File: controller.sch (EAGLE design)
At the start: 47 parts, among them IC1 7805DT, Q3 MOSFET-NCHANNELFDD8780, Q5 MMBT4403, SW1 ROTARTY_ENCODER, U1 ATMEGA328P, Y1 16MHz

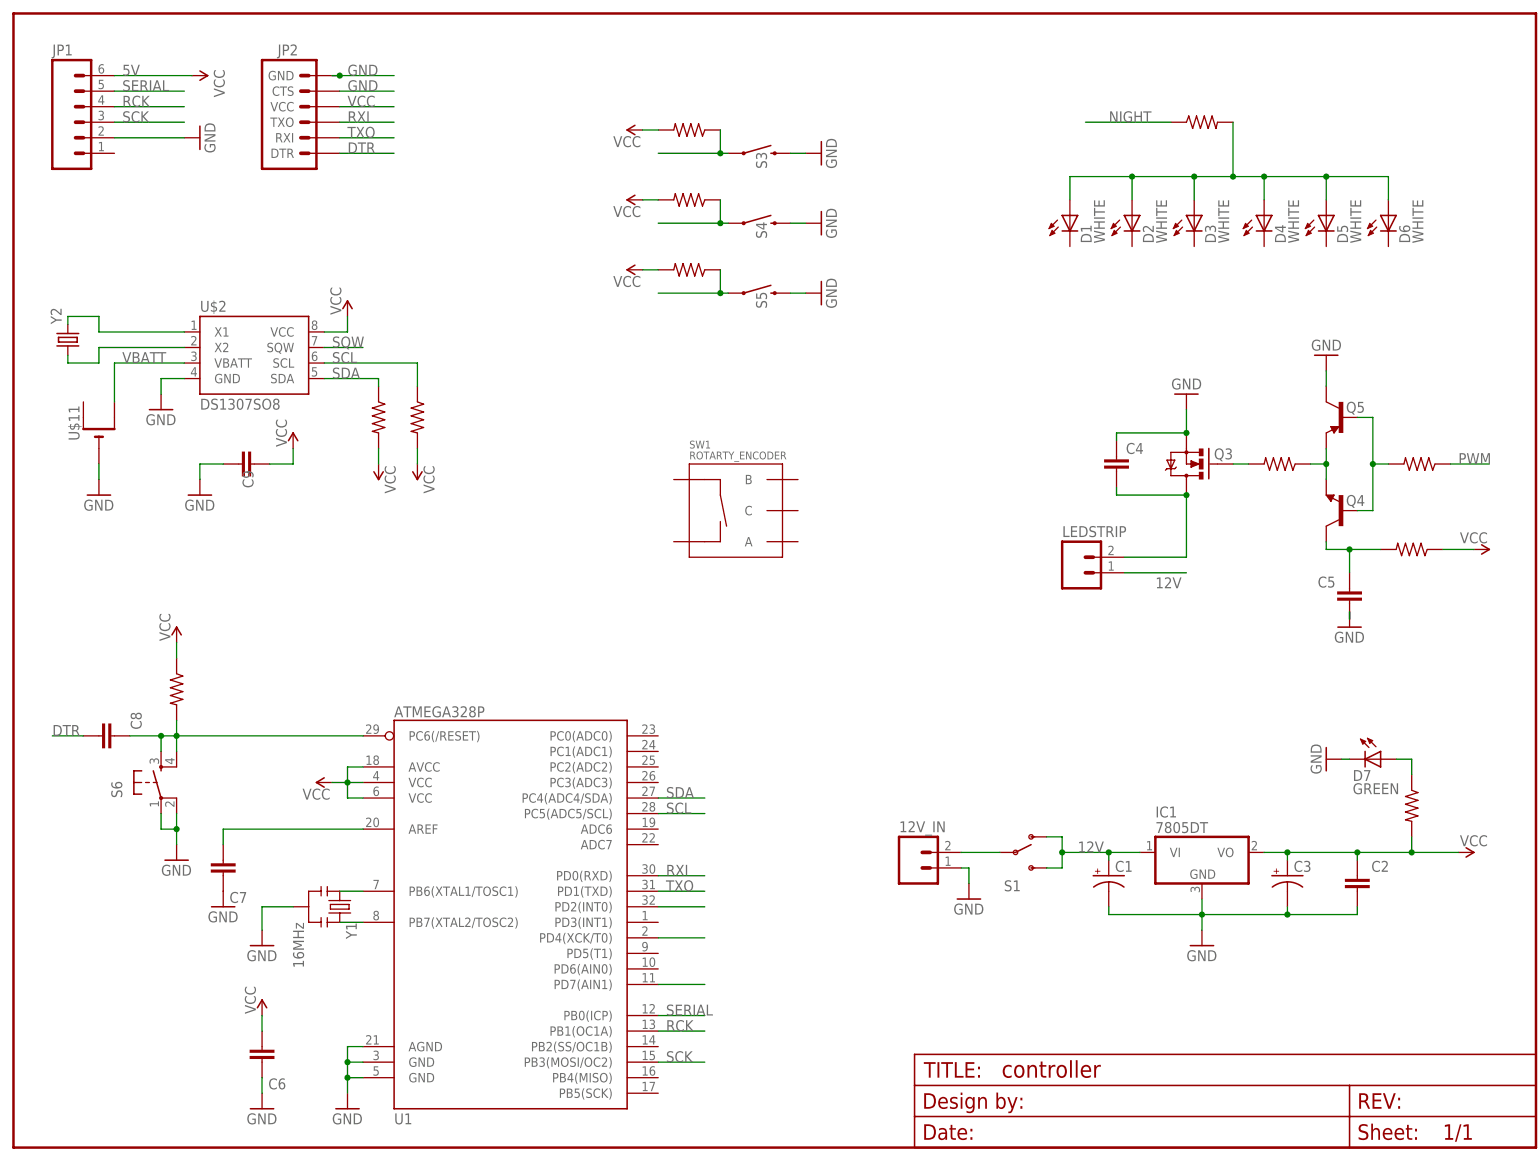
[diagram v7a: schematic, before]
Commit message: Layed out micro, jumpers, and rtc section.
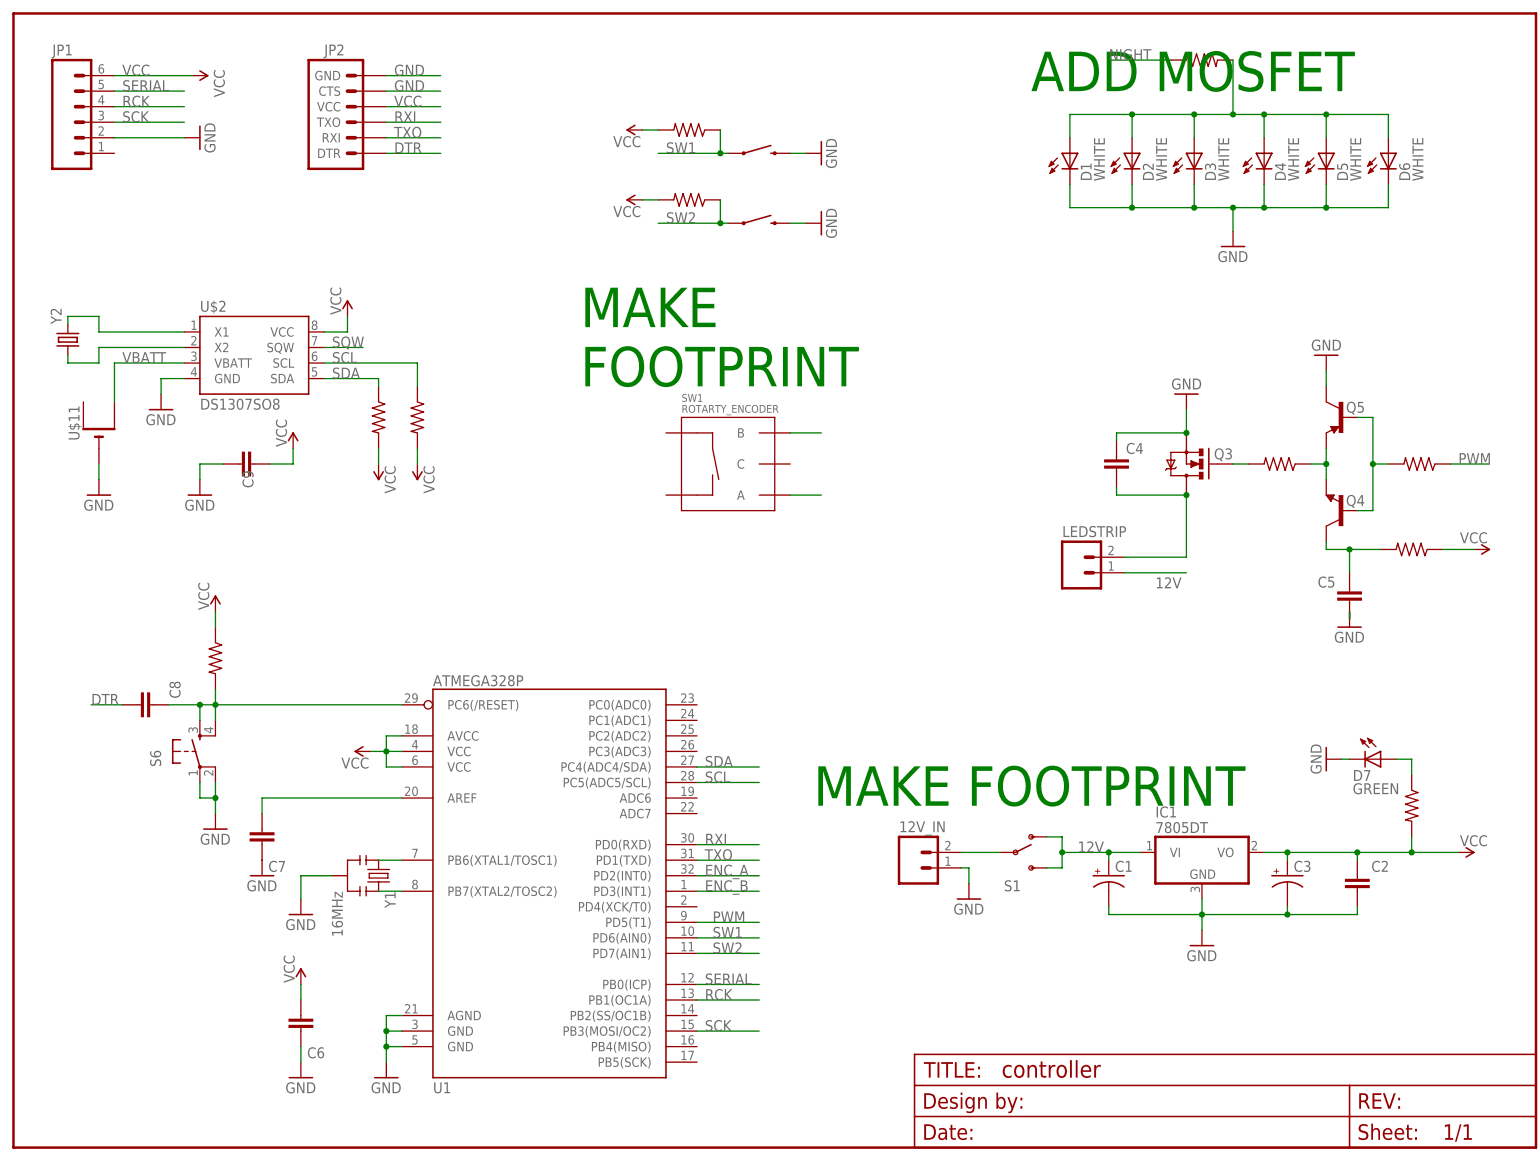
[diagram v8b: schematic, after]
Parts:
- removed S5: SWITCH-MOMENTARY-2SIDE_EZ, SparkFun-Electromechanical:SWITCH-MOMENTARY-2SIDE_EZ
- removed U$15: (no value), jt_parts:RESISTOR
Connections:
- removed net N$13: S3.1, U$12.1
- removed net N$16: S4.1, U$14.1
- removed net N$17: S5.1, U$15.1
- removed net N$18: U1.PD2(INT0)
- removed net N$19: U1.PD4(XCK/T0)
- removed net N$20: U1.PD7(AIN1)
- new net ENC_A: SW1.A, U1.PD2(INT0)
- new net ENC_B: SW1.B, U1.PD3(INT1)
- new net SW1: S3.1, U$12.1, U1.PD6(AIN0)
- new net SW2: S4.1, U$14.1, U1.PD7(AIN1)
- net 5V: no longer JP1.6, U$15.2
- net GND: now also D1.C, D2.C, D3.C, D4.C, D5.C, D6.C; no longer S5.2
- net PWM: now also U1.PD5(T1)
- net VCC: now also JP1.6
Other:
- note added: "ADD MOSFET"
- note added: "MAKE FOOTPRINT"
- moved on the sheet: C6, C7, C8, D1, D2, D3, D4, D5, D6, JP2, S6, SW1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
